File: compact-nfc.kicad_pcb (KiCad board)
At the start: 2 copper layers, 50 x 50 mm, 42 parts, among them Q1 2N7002, Q2 2N7002, U1 ITR9702, U2 PN5321A3HN_C1xx, Y1 Crystal_GND24

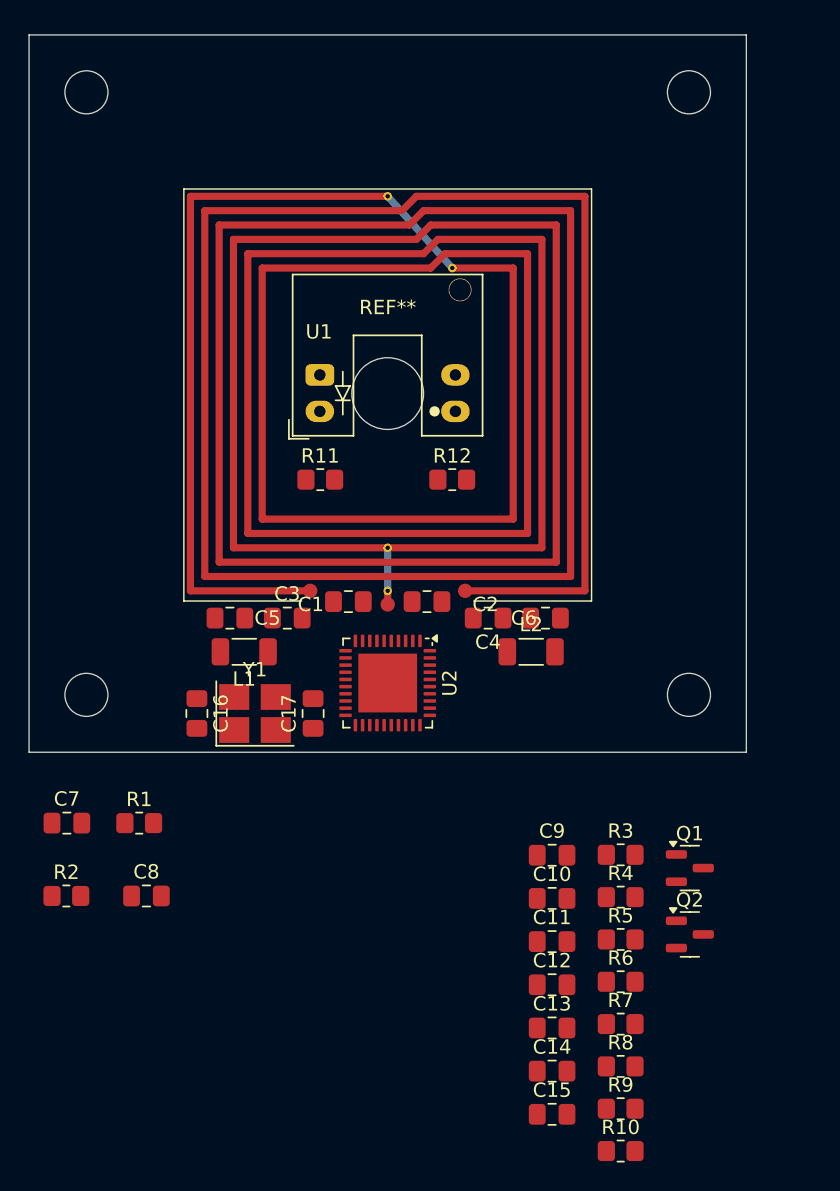
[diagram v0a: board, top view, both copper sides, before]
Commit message: Add debug connector and start manual routing of critical RF coupling network sections
- Added debug connector to schematic and PCB
- Started manual routing of critical RF coupling network components
- Updated footprint library table
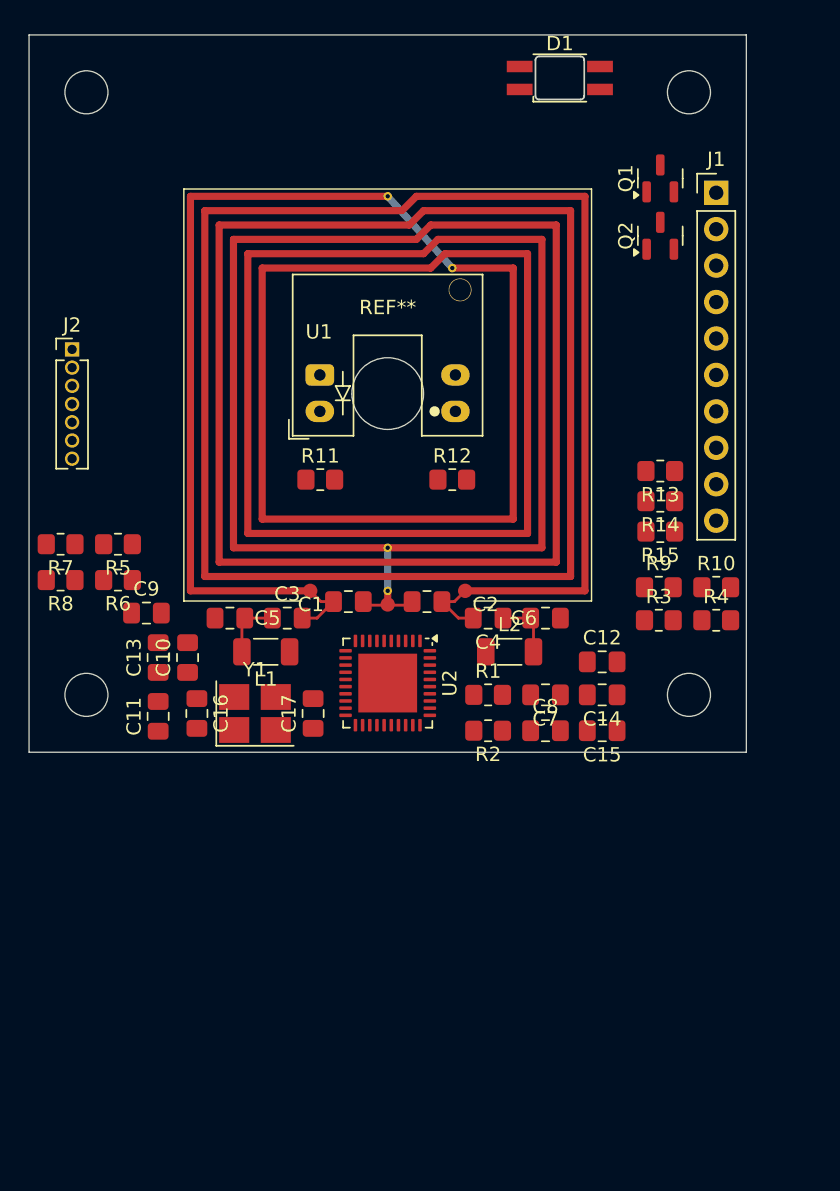
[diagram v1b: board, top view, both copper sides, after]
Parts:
- added D1: LED_RAGB, LED_SMD_REVERSE_MOUNT:LED_RGB_SMD_6028_2.8x3.5mm_Square, F.Cu at (137.0, 103.0)
- added J1: Conn_01x10_Pin, Connector_PinHeader_2.54mm:PinHeader_1x10_P2.54mm_Vertical, F.Cu at (147.9, 111.0)
- added J2: Conn_01x07_Pin, Connector_PinHeader_1.27mm:PinHeader_1x07_P1.27mm_Vertical, F.Cu at (103.0, 121.9)
- added R13: R, Resistor_SMD:R_0805_2012Metric_Pad1.20x1.40mm_HandSolder, F.Cu at (144.0, 130.4)
- added R14: R, Resistor_SMD:R_0805_2012Metric_Pad1.20x1.40mm_HandSolder, F.Cu at (144.0, 132.5)
- added R15: R, Resistor_SMD:R_0805_2012Metric_Pad1.20x1.40mm_HandSolder, F.Cu at (144.0, 134.6)
- moved R8 51.7 mm to (102.2, 138.0), turned to 180 degrees
- moved R7 51.4 mm to (102.2, 135.5), turned to 180 degrees
- moved Q2 48.7 mm to (144.0, 114.0), turned to 90 degrees
- moved Q1 48.1 mm to (144.0, 110.0), turned to 90 degrees
- moved R6 44.9 mm to (106.2, 138.0), turned to 180 degrees
- moved R5 44.6 mm to (106.2, 135.5), turned to 180 degrees
- moved R10 39.9 mm to (147.9, 138.5)
- moved C13 37.7 mm to (109.0, 143.4), turned to 90 degrees
- moved R9 36.4 mm to (143.9, 138.5)
- moved C7 34.5 mm to (136.0, 146.0), turned to 180 degrees
- moved C9 32.9 mm to (108.2, 140.3)
- moved C11 31.6 mm to (109.0, 147.5), turned to 90 degrees
- moved R2 31.6 mm to (132.0, 148.5), turned to 180 degrees
- moved C10 30.5 mm to (111.0, 143.4), turned to 90 degrees
- moved C8 30.1 mm to (136.0, 148.5)
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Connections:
- net Net-(R12-Pad1) renamed /SENS_DET
- net Net-(U2-~{RSTPD}) renamed /RSTPD_N
- Q1 pad 3: unconnected-(Q1-D-Pad3) -> Net-(J1-Pin_1)
- Q2 pad 3: unconnected-(Q2-D-Pad3) -> Net-(J1-Pin_2)
- R11 pad 1: unconnected-(R11-Pad1) -> /SENS_LED
- R12 pad 2: unconnected-(R12-Pad2) -> VCC
- U2 pad 12: unconnected-(U2-AUX1-Pad12) -> /AUX1
- U2 pad 13: unconnected-(U2-AUX2-Pad13) -> /AUX2
- U2 pad 24: unconnected-(U2-P30/UART_RX-Pad24) -> /UART_RX
- U2 pad 25: unconnected-(U2-P70_IRQ-Pad25) -> /IRQ
- U2 pad 29: unconnected-(U2-MISO/P71-Pad29) -> /CIPO
- U2 pad 30: unconnected-(U2-SCK/P72-Pad30) -> /SCK
- U2 pad 31: unconnected-(U2-P31/UART_TX-Pad31) -> /UART_TX
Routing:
- net Net-(C4-Pad1): track 0.00 -> 4.36 mm
- net Net-(C3-Pad1): track 0.00 -> 4.36 mm
- net Net-(C1-Pad1): track 0.00 -> 4.04 mm
- net Net-(C2-Pad2): track 0.00 -> 4.04 mm
- net GND: track 0.00 -> 3.61 mm

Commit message: Complete main trace routing
- Finished main trace routing for PCB layout
- Updated schematic and project files
- Updated backup files
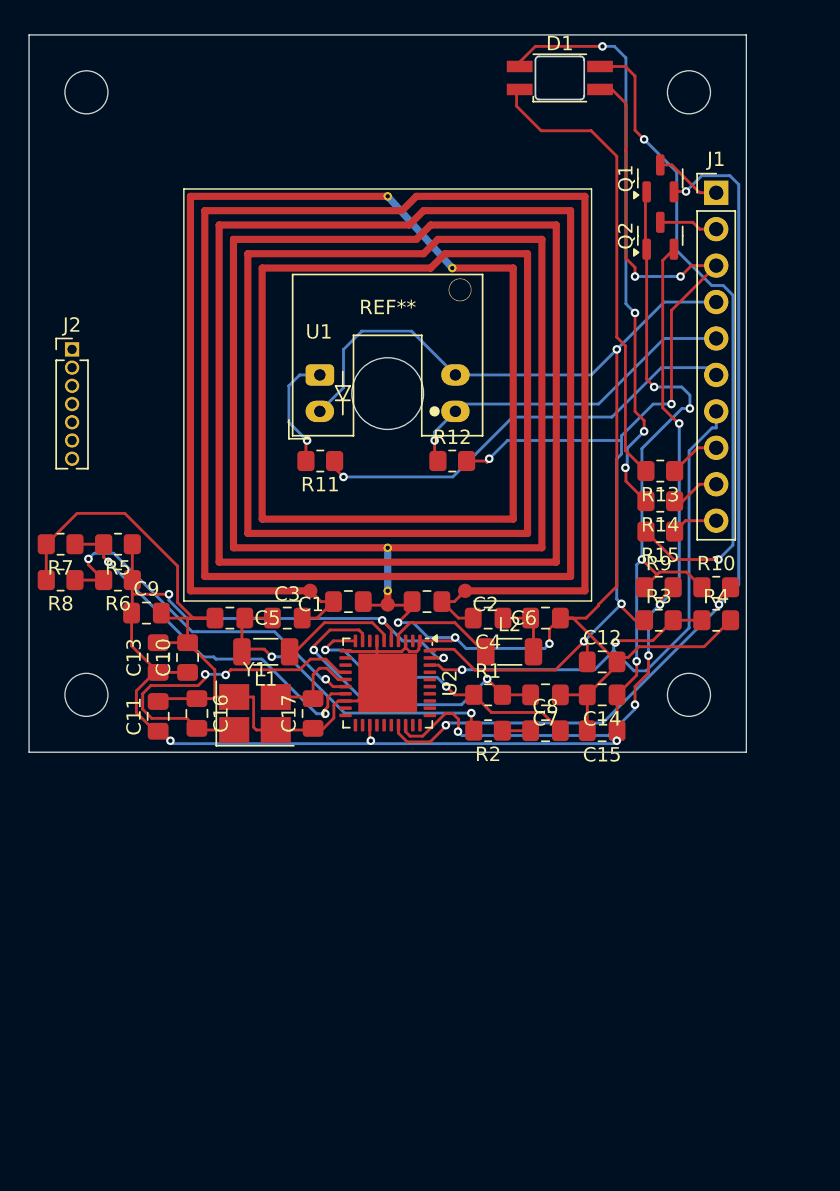
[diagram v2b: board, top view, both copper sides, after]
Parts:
- moved R11 1.30 mm to (120.3, 129.7), turned to 180 degrees
- moved R12 1.30 mm to (129.5, 129.7)
- renumbered REF** to MH1, REF** to MH2, REF** to MH3, REF** to MH4
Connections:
- J1 pad 5: /SENS_LED -> /SENS_DET
- J1 pad 6: /SENS_DET -> /SENS_LED
- J2 pad 1: /AUX1 -> unconnected-(J2-Pin_1-Pad1)
- J2 pad 2: /AUX2 -> unconnected-(J2-Pin_2-Pad2)
- J2 pad 3: /IRQ -> unconnected-(J2-Pin_3-Pad3)
- J2 pad 4: /CIPO -> unconnected-(J2-Pin_4-Pad4)
- J2 pad 5: /SCK -> unconnected-(J2-Pin_5-Pad5)
- J2 pad 6: /UART_RX -> unconnected-(J2-Pin_6-Pad6)
- J2 pad 7: /UART_TX -> unconnected-(J2-Pin_7-Pad7)
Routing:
- net GND: track 3.61 -> 162.3 mm, vias 0 -> 4
- net +3.3V: track 0.00 -> 127.1 mm, vias 0 -> 10
- net VCC: track 0.00 -> 78.5 mm, vias 0 -> 6
- net Net-(Q1-S): track 0.00 -> 63.9 mm, vias 0 -> 3
- net Net-(Q2-S): track 0.00 -> 54.9 mm, vias 0 -> 5
- net Net-(D1-BK): track 0.00 -> 46.0 mm, vias 0 -> 2
- net /RSTPD_N: track 0.00 -> 43.9 mm, vias 0 -> 2
- net Net-(D1-GK): track 0.00 -> 41.1 mm, vias 0 -> 4
- net Net-(D1-RK): track 0.00 -> 32.5 mm
- net /SENS_LED: track 0.00 -> 30.7 mm, vias 0 -> 1
- net Net-(U2-I0): track 0.00 -> 25.9 mm, vias 0 -> 2
- net Net-(U2-I1): track 0.00 -> 25.4 mm, vias 0 -> 2
- net /SENS_DET: track 0.00 -> 24.4 mm, vias 0 -> 1
- net Net-(U2-OSCIN): track 0.00 -> 23.8 mm, vias 0 -> 2
- net Net-(U2-VMID): track 0.00 -> 22.7 mm, vias 0 -> 2
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
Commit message: Organize silkscreen labels for component assembly identification
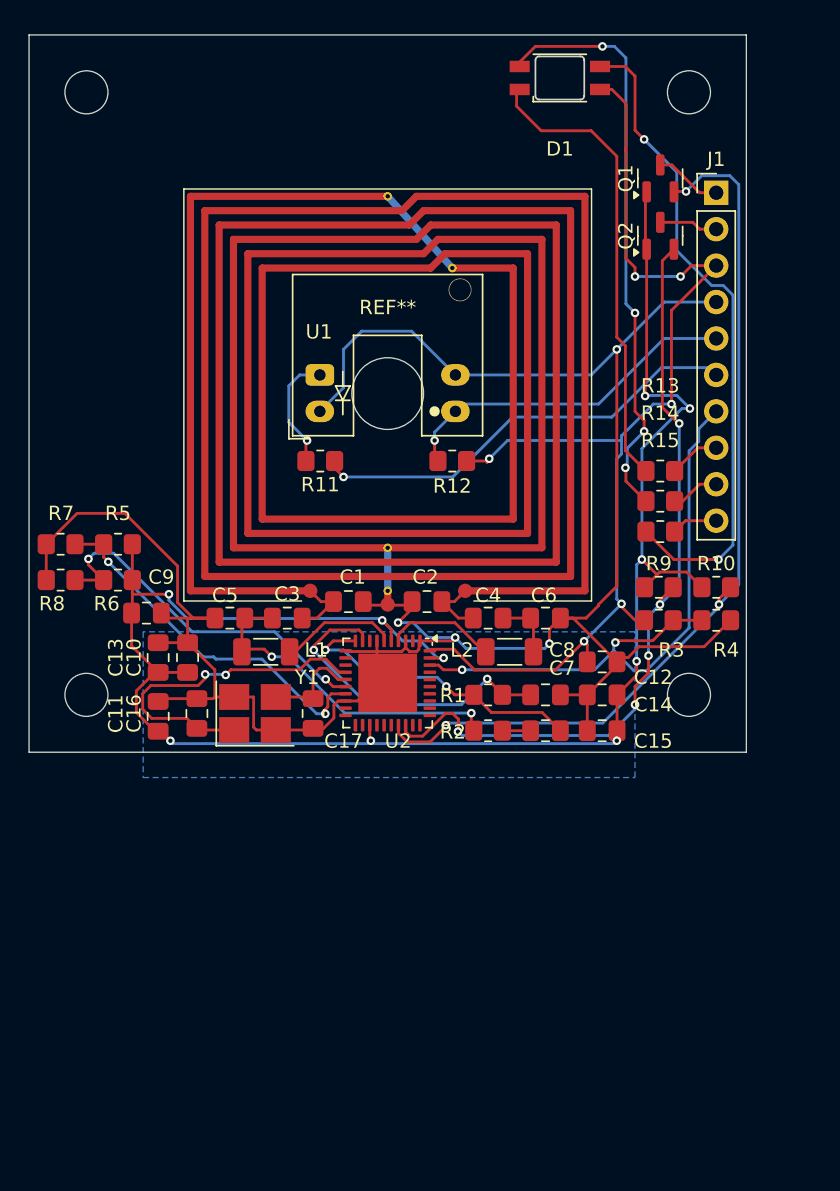
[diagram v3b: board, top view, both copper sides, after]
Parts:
- removed J2: Conn_01x07_Pin, Connector_PinHeader_1.27mm:PinHeader_1x07_P1.27mm_Vertical
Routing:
- added copper zone on B.Cu, net GND

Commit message: Add Gerber files for single-card PCB
Generated Gerber outputs for the compact NFC single-card PCB design,
including copper layers, mask, paste, silkscreen, drill files and
the single-board export zip.
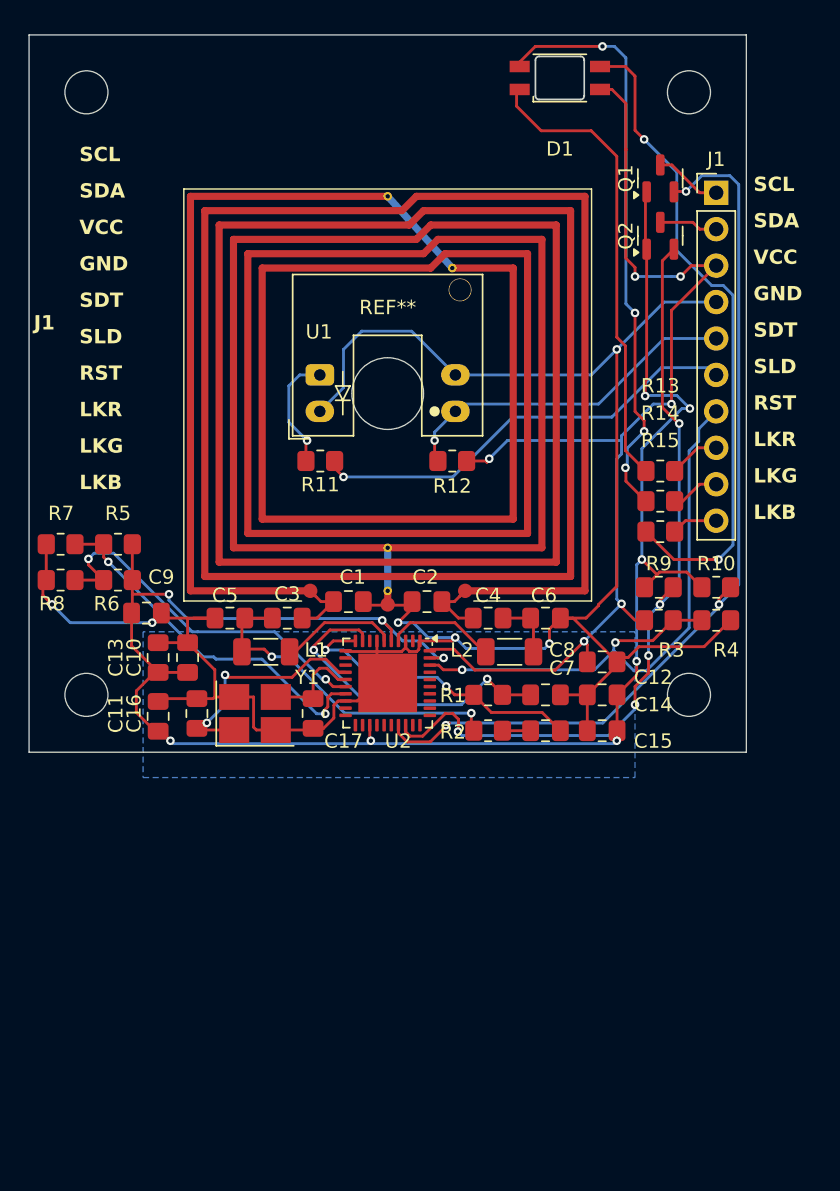
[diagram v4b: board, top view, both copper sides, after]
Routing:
- net Net-(U2-OSCIN): track 23.8 -> 16.7 mm
- net GND: track 162.3 -> 157.1 mm, vias 4 -> 6
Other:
- board text added: "GND"
- board text added: "J1"
- board text added: "LKB"
- board text added: "LKG"
- board text added: "LKR"
- board text added: "RST"
- board text added: "SCL"
- board text added: "SDA"
- board text added: "SDT"
- board text added: "SLD"
- board text added: "VCC"

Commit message: Fix silkscreen layer issues
Silkscreen adjustments and corrections on the PCB design.
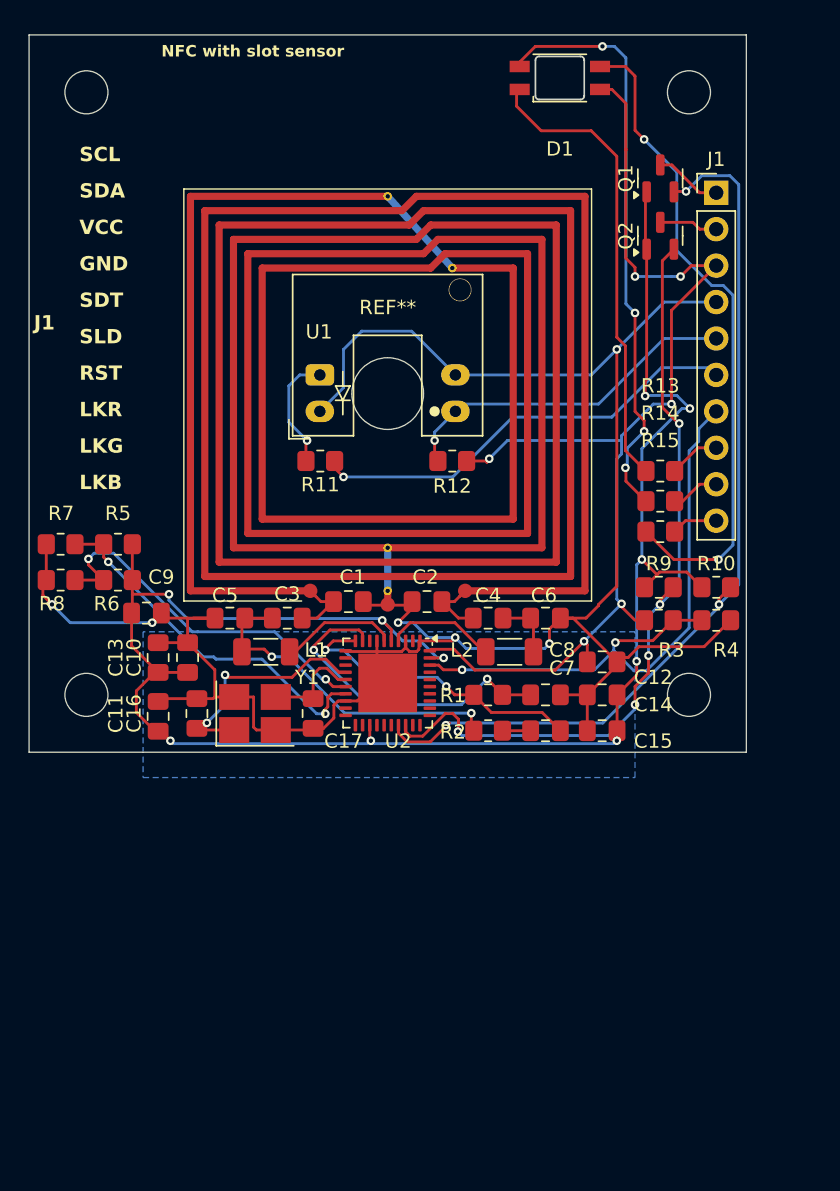
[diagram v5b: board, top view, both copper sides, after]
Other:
- board text added: "NFC with slot sensor"
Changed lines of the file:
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@@
-    (effects (font (size 1 1) (thickness 0.25) bold) (justify left bottom))
-  )
-  (gr_text "SCL" (at 150.495 111) (layer "F.SilkS")
     (effects (font (size 1 1) (thickness 0.25) bold) (justify left bottom))
   )
   (gr_text "GND" (at 103.505 116.54) (layer "F.SilkS")
-    (effects (font (size 1 1) (thickness 0.25) bold) (justify left bottom))
-  )
-  (gr_text "LKR" (at 150.495 128.78) (layer "F.SilkS")
     (effects (font (size 1 1) (thickness 0.25) bold) (justify left bottom))
   )
@@
     (effects (font (size 1 1) (thickness 0.25) bold) (justify left bottom))
   )
-  (gr_text "SDT" (at 150.495 121.16) (layer "F.SilkS")
-    (effects (font (size 1 1) (thickness 0.25) bold) (justify left bottom))
-  )
   (gr_text "RST" (at 103.505 124.16) (layer "F.SilkS")
     (effects (font (size 1 1) (thickness 0.25) bold) (justify left bottom))
@@
     (effects (font (size 1 1) (thickness 0.25) bold) (justify left bottom))
   )
-  (gr_text "VCC" (at 150.495 116.08) (layer "F.SilkS")
-    (effects (font (size 1 1) (thickness 0.25) bold) (justify left bottom))
-  )
-  (gr_text "SLD" (at 150.495 123.7) (layer "F.SilkS")
-    (effects (font (size 1 1) (thickness 0.25) bold) (justify left bottom))
-  )
-  (gr_text "RST" (at 150.495 126.24) (layer "F.SilkS")
-    (effects (font (size 1 1) (thickness 0.25) bold) (justify left bottom))
-  )
   (gr_text "SDT" (at 103.505 119.08) (layer "F.SilkS")
-    (effects (font (size 1 1) (thickness 0.25) bold) (justify left bottom))
-  )
-  (gr_text "LKB" (at 150.495 133.86) (layer "F.SilkS")
-    (effects (font (size 1 1) (thickness 0.25) bold) (justify left bottom))
-  )
-  (gr_text "LKG" (at 150.495 131.32) (layer "F.SilkS")
     (effects (font (size 1 1) (thickness 0.25) bold) (justify left bottom))
   )
@@
     (effects (font (size 1 1) (thickness 0.25) bold) (justify left bottom))
   )
-  (gr_text "SDA" (at 150.495 113.54) (layer "F.SilkS")
-    (effects (font (size 1 1) (thickness 0.25) bold) (justify left bottom))
-  )
-  (gr_text "GND" (at 150.495 118.62) (layer "F.SilkS")
-    (effects (font (size 1 1) (thickness 0.25) bold) (justify left bottom))
+  (gr_text "NFC with slot sensor" (at 109.22 101.6) (layer "F.SilkS")
+    (effects (font (size 0.8 0.8) (thickness 0.2) bold) (justify left bottom))
   )
   (segment (start 144.8106 109.0625) (end 146.7481 111) (width 0.2) (layer "F.Cu") (net 1))
